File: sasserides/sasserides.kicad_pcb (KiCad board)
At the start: 2 copper layers, 170 x 80 mm, 128 parts, among them J1 Conn_02x16_Odd_Even, Q1 2N7002

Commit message: Apply OSH Park stackups and design rules.
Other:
- rule pad_to_mask_clearance: 0 -> 0.0508
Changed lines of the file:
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@@
 (kicad_pcb (version 20221018) (generator pcbnew)
   (general
-    (thickness 1.6)
+    (thickness 1.646)
   )
   (paper "A4")
@@
   )
   (setup
-    (pad_to_mask_clearance 0)
+    (stackup
+      (layer "F.SilkS" (type "Top Silk Screen"))
+      (layer "F.Paste" (type "Top Solder Paste"))
+      (layer "F.Mask" (type "Top Solder Mask") (color "Purple") (thickness 0.0254) (material "Liquid Ink") (epsilon_r 3.3) (loss_tangent 0))
+      (layer "F.Cu" (type "copper") (thickness 0.0356))
+      (layer "dielectric 1" (type "core") (color "FR4 natural") (thickness 1.524) (material "FR4") (epsilon_r 4.6) (loss_tangent 0.016))
+      (layer "B.Cu" (type "copper") (thickness 0.0356))
+      (layer "B.Mask" (type "Bottom Solder Mask") (color "Purple") (thickness 0.0254) (material "Liquid Ink") (epsilon_r 3.3) (loss_tangent 0))
+      (layer "B.Paste" (type "Bottom Solder Paste"))
+      (layer "B.SilkS" (type "Bottom Silk Screen"))
+      (copper_finish "None")
+      (dielectric_constraints no)
+    )
+    (pad_to_mask_clearance 0.0508)
+    (solder_mask_min_width 0.1016)
     (pcbplotparams
       (layerselection 0x00010fc_ffffffff)

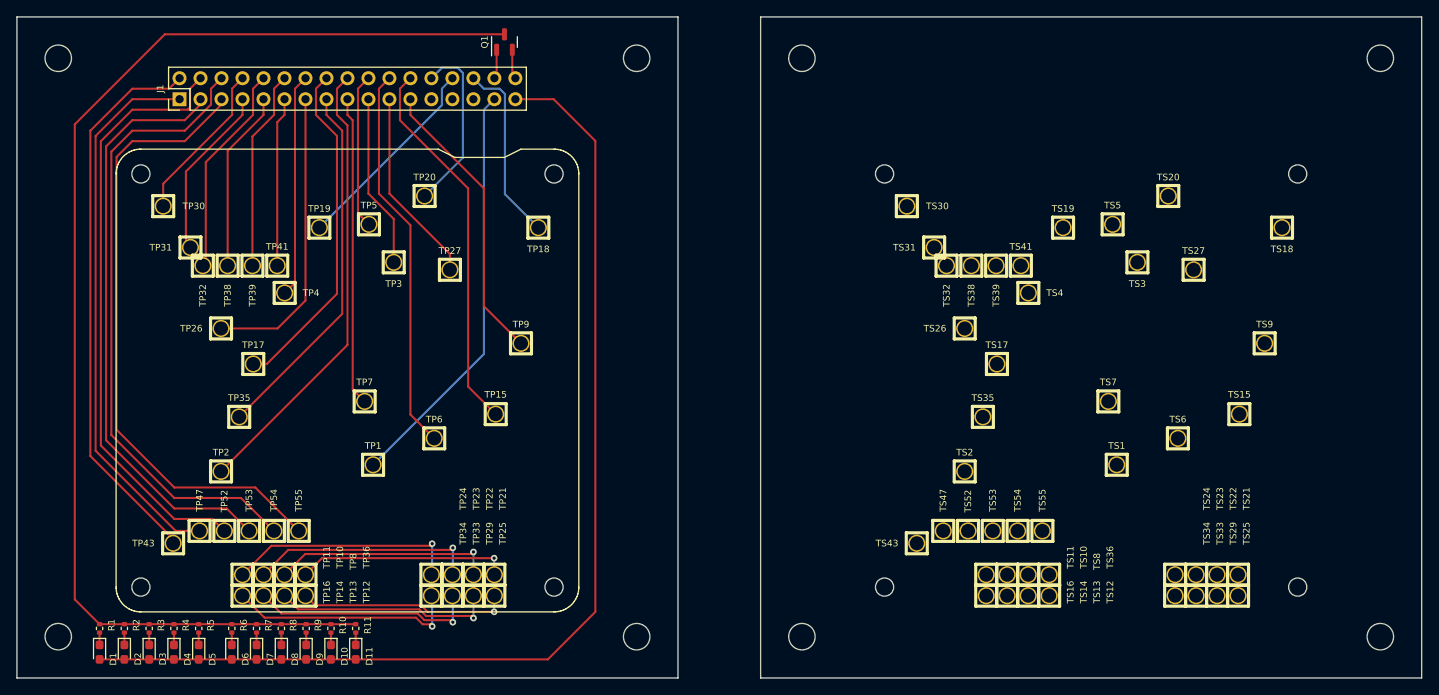
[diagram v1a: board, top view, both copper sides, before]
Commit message: Add labels to Sasserides silkscreen
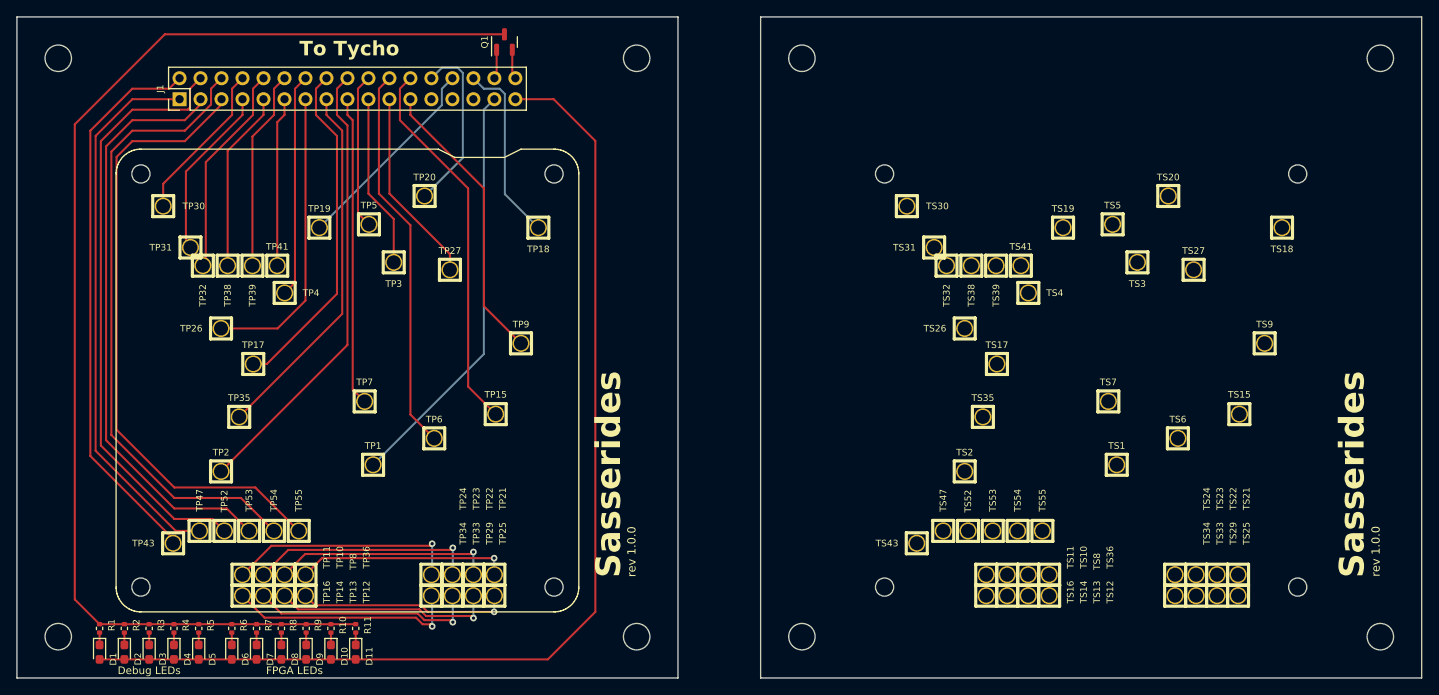
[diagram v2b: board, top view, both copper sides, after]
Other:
- board text added: "Debug LEDs"
- board text added: "FPGA LEDs"
- board text added: "Sasserides"
- board text added: "To Tycho"
- board text added: "rev 1.0.0"
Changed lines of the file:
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@@
   (gr_rect (start 60 60) (end 140 140)
     (stroke (width 0.1) (type default)) (fill none) (layer "Edge.Cuts"))
+  (gr_text "rev 1.0.0" (at 134.98 127.79 90) (layer "F.SilkS")
+    (effects (font (size 1 1) (thickness 0.15)) (justify left bottom))
+  )
+  (gr_text "rev 1.0.0" (at 225.04 127.75 90) (layer "F.SilkS")
+    (effects (font (size 1 1) (thickness 0.15)) (justify left bottom))
+  )
+  (gr_text "Sasserides" (at 223.34 127.89 90) (layer "F.SilkS")
+    (effects (font (size 3 3) (thickness 0.5) bold) (justify left bottom))
+  )
+  (gr_text "Sasserides" (at 133.35 127.88 90) (layer "F.SilkS")
+    (effects (font (size 3 3) (thickness 0.5) bold) (justify left bottom))
+  )
+  (gr_text "To Tycho" (at 94.18 64.86) (layer "F.SilkS")
+    (effects (font (size 1.75 1.75) (thickness 0.3) bold) (justify left bottom))
+  )
+  (gr_text "FPGA LEDs" (at 93.59 139.1) (layer "F.SilkS")
+    (effects (font (size 0.9144 0.9238) (thickness 0.15)))
+  )
+  (gr_text "Debug LEDs" (at 76 139.1) (layer "F.SilkS")
+    (effects (font (size 0.9144 0.9144) (thickness 0.15)))
+  )
   (segment (start 70 136) (end 70 134.51) (width 0.25) (layer "F.Cu") (net 1))
   (segment (start 124.25 137.75) (end 130 132) (width 0.25) (layer "F.Cu") (net 2))

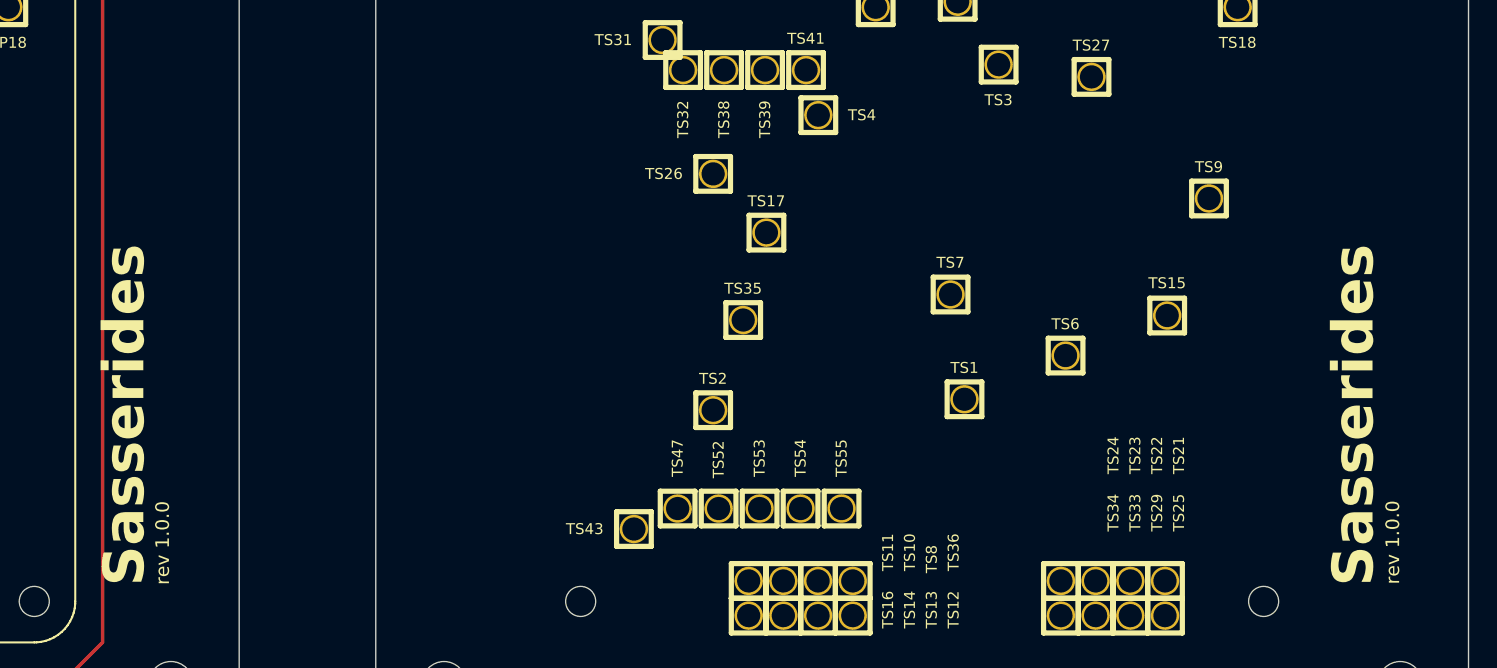
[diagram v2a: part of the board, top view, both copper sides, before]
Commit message: Label Sasserides boards as A & B
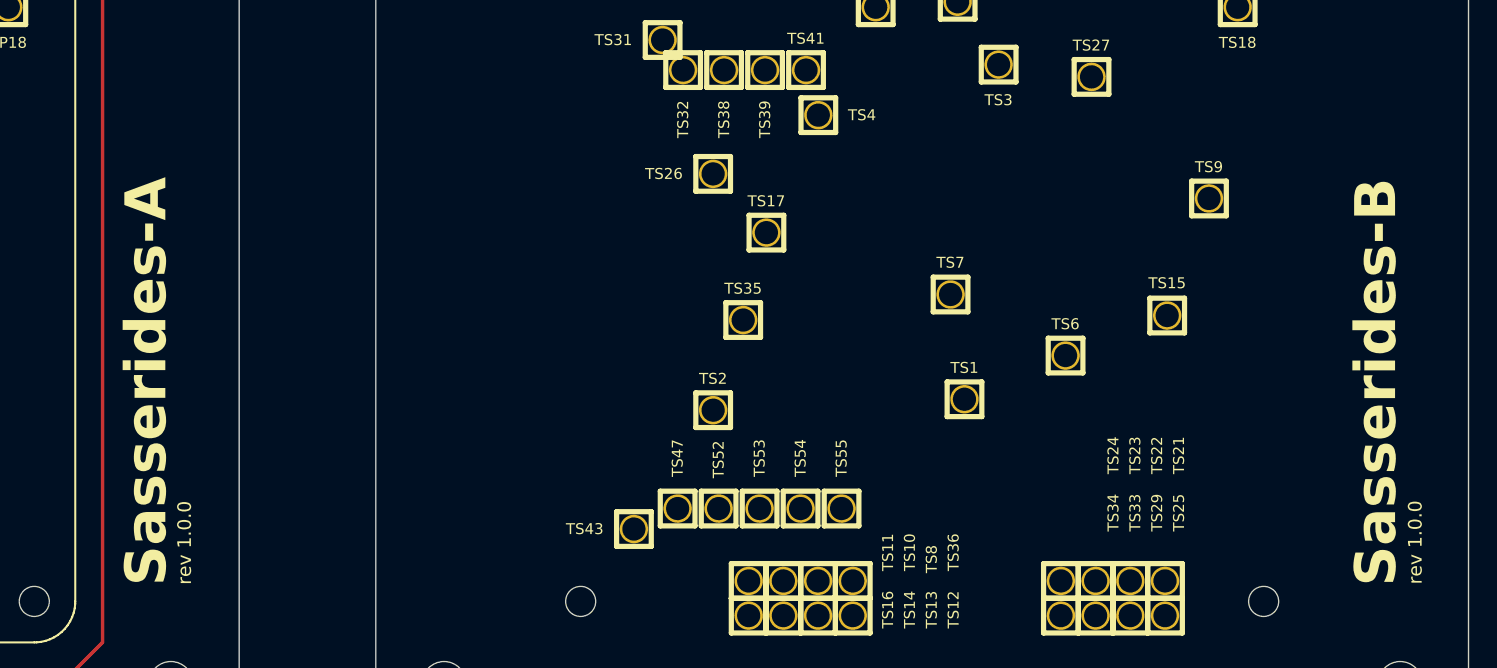
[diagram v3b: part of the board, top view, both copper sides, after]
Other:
- board text added: "Sasserides-A"
- board text added: "Sasserides-B"
- board text removed: "Sasserides"
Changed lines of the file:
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@@
   (gr_rect (start 60 60) (end 140 140)
     (stroke (width 0.1) (type default)) (fill none) (layer "Edge.Cuts"))
-  (gr_text "rev 1.0.0" (at 134.98 127.79 90) (layer "F.SilkS")
+  (gr_text "rev 1.0.0" (at 136.59 127.78 90) (layer "F.SilkS")
     (effects (font (size 1 1) (thickness 0.15)) (justify left bottom))
   )
-  (gr_text "rev 1.0.0" (at 225.04 127.75 90) (layer "F.SilkS")
+  (gr_text "rev 1.0.0" (at 226.69 127.75 90) (layer "F.SilkS")
     (effects (font (size 1 1) (thickness 0.15)) (justify left bottom))
   )
-  (gr_text "Sasserides" (at 223.34 127.89 90) (layer "F.SilkS")
+  (gr_text "Sasserides-B" (at 224.99 127.89 90) (layer "F.SilkS")
     (effects (font (size 3 3) (thickness 0.5) bold) (justify left bottom))
   )
-  (gr_text "Sasserides" (at 133.35 127.88 90) (layer "F.SilkS")
+  (gr_text "Sasserides-A" (at 134.96 127.87 90) (layer "F.SilkS")
     (effects (font (size 3 3) (thickness 0.5) bold) (justify left bottom))
   )

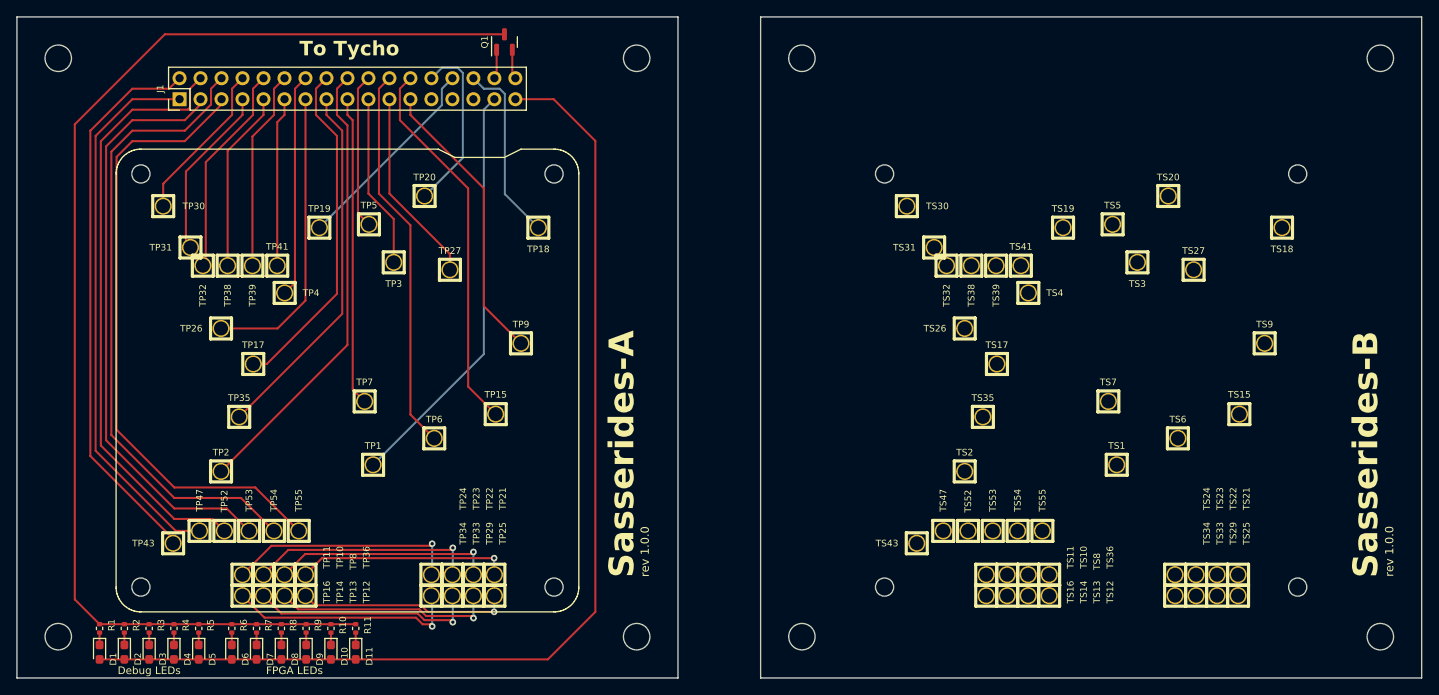
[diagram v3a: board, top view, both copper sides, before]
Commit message: Fix test points
	*Move TP7, TP9, & TP15 to correct locations
	*Swap TARGET_A_VBUS AND AUX_PHY_3V3 on MUX1
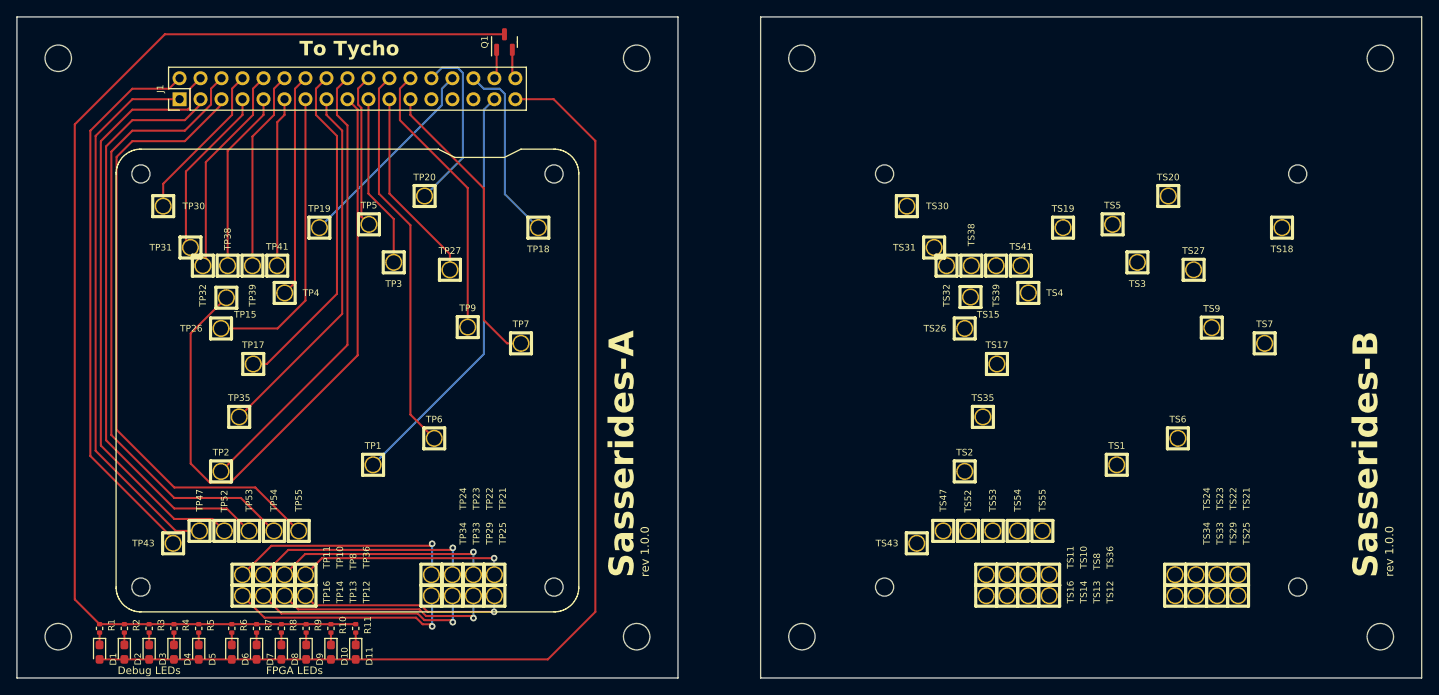
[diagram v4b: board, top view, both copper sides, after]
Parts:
- added ?: , , F.Cu at (175.4, 93.9)
- added ?: , , F.Cu at (211.0, 99.5)
- added TP15: TestPoint, TestPoint:TestPoint_Pad_D1.0mm, B.Cu at (85.4, 93.9)
- added TP7: TestPoint, TestPoint:TestPoint_Pad_D1.0mm, B.Cu at (121.0, 99.5)
- added TP9: TestPoint, TestPoint:TestPoint_Pad_D1.0mm, B.Cu at (114.6, 97.6)
- added TP9: TestPoint, TestPoint:TestPoint_Pad_D1.0mm, B.Cu at (204.6, 97.6)
- moved TP15 35.5 mm to (85.3, 94.0)
- moved TS15 35.5 mm to (175.4, 93.9)
- moved TP7 20.2 mm to (121.0, 99.5)
- moved TS7 20.2 mm to (211.0, 99.5)
- moved TP9 6.74 mm to (114.6, 97.5)
- moved TS9 6.68 mm to (204.6, 97.6)
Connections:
- TP15 pad 1: Net-(J1-Pin_24) -> Net-(J1-Pin_17)
- TP7 pad 1: Net-(J1-Pin_17) -> Net-(J1-Pin_23)
- TP9 pad 1: Net-(J1-Pin_23) -> Net-(J1-Pin_24)
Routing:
- net Net-(J1-Pin_17): track 37.4 -> 80.9 mm
- net Net-(J1-Pin_24): track 46.0 -> 34.0 mm
- net Net-(J1-Pin_23): track 35.1 -> 36.1 mm

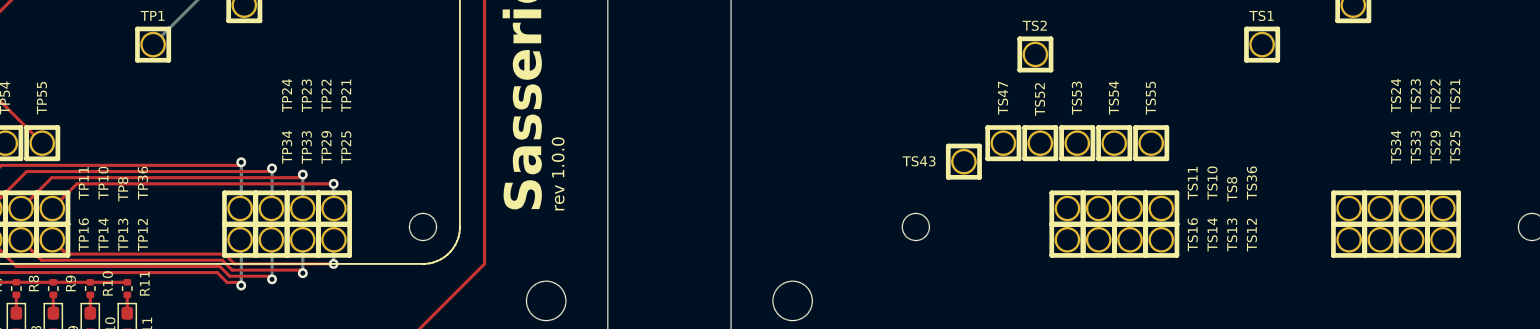
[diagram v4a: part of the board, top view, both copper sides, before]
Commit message: Rename Pmod TPs to A0-7/B0-7
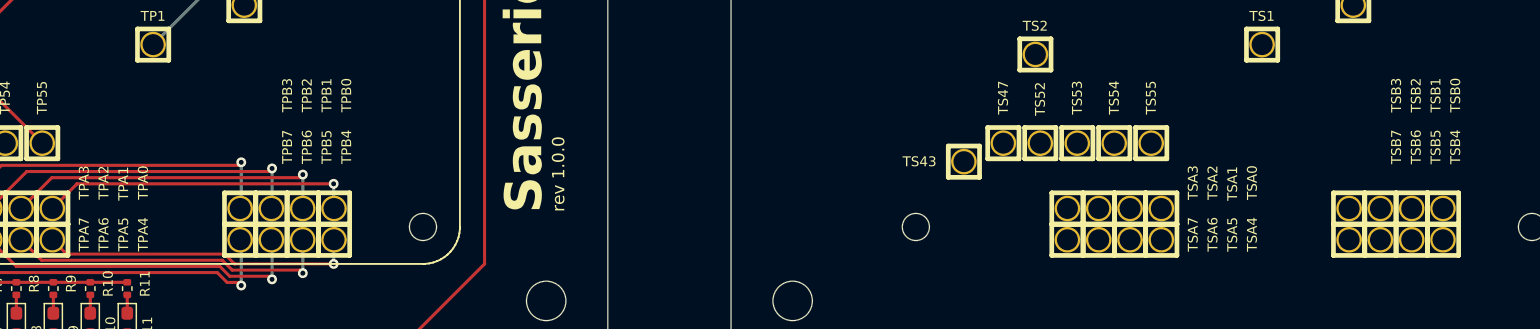
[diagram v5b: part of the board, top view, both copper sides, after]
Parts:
- renumbered TP36 to TPA0, TP8 to TPA1, TP10 to TPA2, TP11 to TPA3, TP12 to TPA4, TP13 to TPA5, TP14 to TPA6, TP16 to TPA7, TP21 to TPB0, TP22 to TPB1, TP23 to TPB2, TP24 to TPB3, TP25 to TPB4, TP29 to TPB5, TP33 to TPB6, TP34 to TPB7, TS36 to TSA0, TS8 to TSA1, TS10 to TSA2, TS11 to TSA3, TS12 to TSA4, TS13 to TSA5, TS14 to TSA6, TS16 to TSA7, TS21 to TSB0, TS22 to TSB1, TS23 to TSB2, TS24 to TSB3, TS25 to TSB4, TS29 to TSB5, TS33 to TSB6, TS34 to TSB7
